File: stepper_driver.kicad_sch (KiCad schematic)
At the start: 7 parts, among them J20 Stepper, U3 TMC2208_SILENTSTEPSTICK

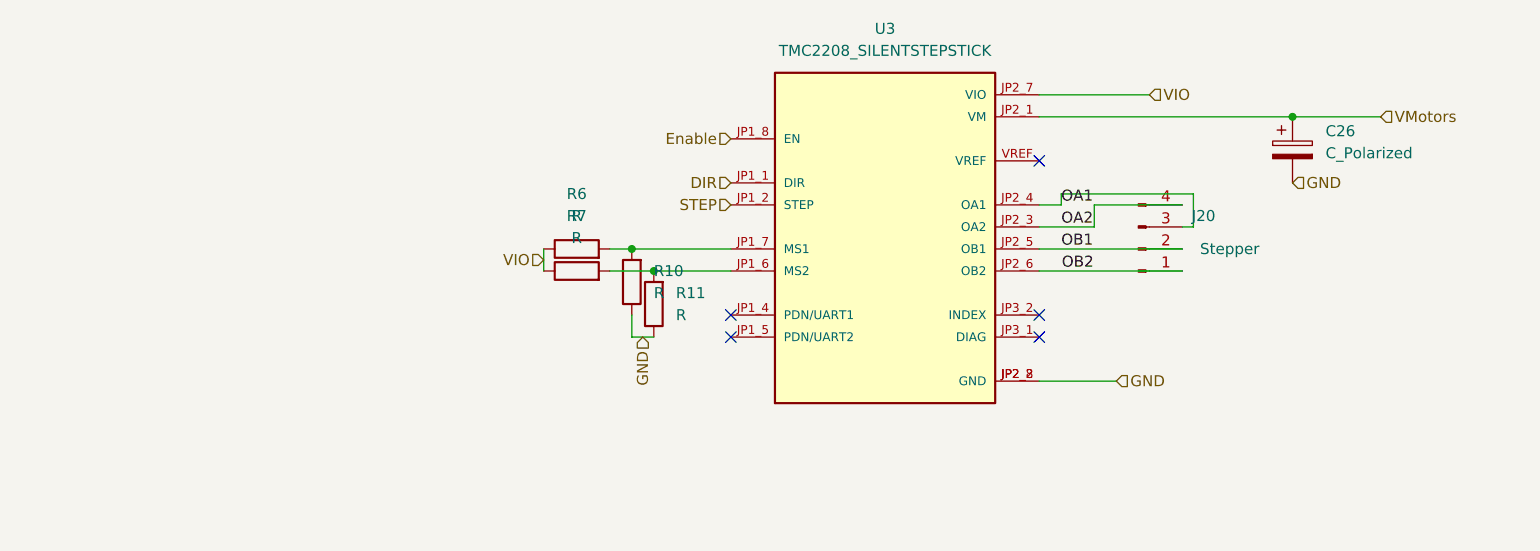
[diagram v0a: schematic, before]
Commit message: fix warnings + add internal layers + add Uart to steppers (TX only
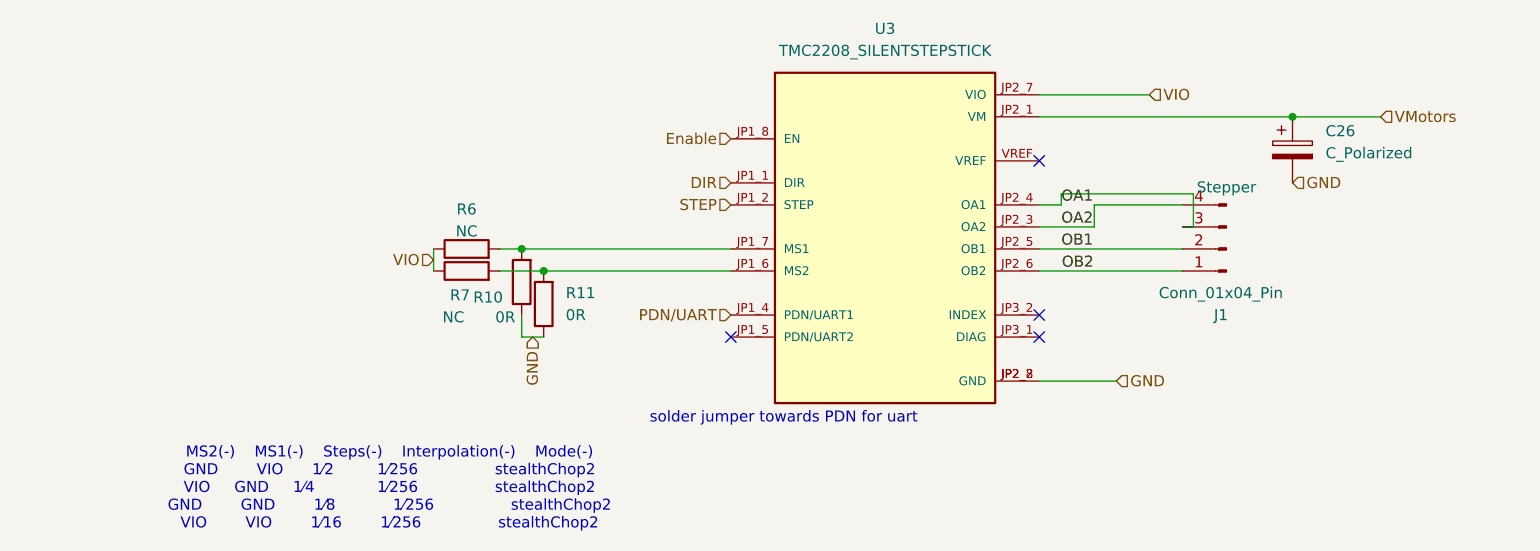
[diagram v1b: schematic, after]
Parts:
- removed J20: Stepper, Connector_JST:JST_XH_B4B-XH-A_1x04_P2.50mm_Vertical, symbol Connector:Conn_01x04_Male
- added J1: Conn_01x04_Pin, Connector_JST:JST_XH_B4B-XH-A_1x04_P2.50mm_Vertical, symbol Connector:Conn_01x04_Pin
- R10, R11: value R -> 0R
- R6, R7: value R -> NC
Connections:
- net OA1: now also J1.3 (Pin_3)
- net OA2: now also J1.4 (Pin_4)
- net OB1: now also J1.2 (Pin_2)
- net OB2: now also J1.1 (Pin_1)
- net PDN/UART: now reaches U3.JP1_4 (PDN/UART1)
- no-connect marks 5 -> 4
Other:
- note added: "MS2(-) MS1(-) Steps(-) Interpolation(-) Mode(-) GND VIO 1⁄2 1⁄256 stealthChop2 VIO GND 1⁄4 1⁄256 stealthChop2 GND GND 1⁄8 1⁄256 stealthChop2 VIO VIO 1⁄16 1⁄256 stealthChop2"
- note added: "solder jumper towards PDN for uart"
- moved on the sheet: R10, R11, R6, R7

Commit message: Add BOM
Add LCSC reference and correct few footprint acording bom
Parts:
- C26: LCSC# (none) -> C398835
- J1: LCSC# (none) -> C595709
- R10, R11: LCSC# (none) -> C21189
- U3: Availability In Stock -> (none); Check_prices https://www.snapeda.com/parts/TMC2208%20SILENTSTEPSTICK/Tri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 -> (none); MANUFACTURER Trinamic Motion -> (none); MF Trinamic Motion -> (none); MP TMC2208 SILENTSTEPSTICK -> (none); Package None -> (none); Price None -> (none); SnapEDA_Link https://www.snapeda.com/parts/TMC2208%20SILENTSTEPSTICK/Tri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 -> (none)
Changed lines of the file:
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@@
 	(label "OB2"
 		(at 130.8735 80.01 0)
-		(fields_autoplaced yes)
 		(effects
 			(font
@@
 	(label "OA1"
 		(at 130.81 72.39 0)
-		(fields_autoplaced yes)
 		(effects
 			(font
@@
 	(label "OA2"
 		(at 130.81 74.93 0)
-		(fields_autoplaced yes)
 		(effects
 			(font
@@
 	(label "OB1"
 		(at 130.81 77.47 0)
-		(fields_autoplaced yes)
 		(effects
 			(font
@@
 		(shape input)
 		(at 92.71 85.09 180)
-		(fields_autoplaced yes)
 		(effects
 			(font
@@
 		(shape input)
 		(at 157.48 69.85 0)
-		(fields_autoplaced yes)
 		(effects
 			(font
@@
 		(shape input)
 		(at 92.71 64.77 180)
-		(fields_autoplaced yes)
 		(effects
 			(font
@@
 		(shape input)
 		(at 140.97 59.69 0)
-		(fields_autoplaced yes)
 		(effects
 			(font
@@
 		(shape input)
 		(at 92.71 72.39 180)
-		(fields_autoplaced yes)
 		(effects
 			(font
@@
 		(shape input)
 		(at 58.42 78.74 180)
-		(fields_autoplaced yes)
 		(effects
 			(font
@@
 		(shape input)
 		(at 92.71 69.85 180)
-		(fields_autoplaced yes)
 		(effects
 			(font
@@
 		(shape input)
 		(at 69.85 87.63 270)
-		(fields_autoplaced yes)
 		(effects
 			(font
@@
 		(shape input)
 		(at 167.64 62.23 0)
-		(fields_autoplaced yes)
 		(effects
 			(font
@@
 		(shape input)
 		(at 137.16 92.71 0)
-		(fields_autoplaced yes)
 		(effects
 			(font
@@
 			)
 		)
+		(property "LCSC#" "C398835"
+			(at 157.48 66.04 0)
+			(effects
+				(font
+					(size 1.27 1.27)
+				)
+				(hide yes)
+			)
+		)
 		(pin "1"
 		)
@@
 		)
 		(property "Description" ""
+			(at 62.23 80.01 0)
+			(effects
+				(font
+					(size 1.27 1.27)
+				)
+				(hide yes)
+			)
+		)
+		(property "LCSC#" ""
 			(at 62.23 80.01 0)
 			(effects
@@
 			)
 		)
+		(property "LCSC#" "C21189"
+			(at 71.12 83.82 0)
+			(effects
+				(font
+					(size 1.27 1.27)
+				)
+				(hide yes)
+			)
+		)
 		(pin "1"
 		)
@@
 			)
 		)
-		(property "MF" "Trinamic Motion"
+		(property "LCSC#" ""
 			(at 110.49 74.93 0)
 			(effects
@@
 					(size 1.27 1.27)
 				)
-				(justify bottom)
-				(hide yes)
-			)
-		)
-		(property "Package" "None"
-			(at 110.49 74.93 0)
-			(effects
-				(font
-					(size 1.27 1.27)
-				)
-				(justify bottom)
-				(hide yes)
-			)
-		)
-		(property "Price" "None"
-			(at 110.49 74.93 0)
-			(effects
-				(font
-					(size 1.27 1.27)
-				)
-				(justify bottom)
-				(hide yes)
-			)
-		)
-		(property "Check_prices" "https://www.snapeda.com/parts/TMC2208%20SILENTSTEPSTICK/Trinamic+Motion+Control+GmbH/view-part/?ref=eda"
-			(at 110.49 74.93 0)
-			(effects
-				(font
-					(size 1.27 1.27)
-				)
-				(justify bottom)
-				(hide yes)
-			)
-		)
-		(property "SnapEDA_Link" "https://www.snapeda.com/parts/TMC2208%20SILENTSTEPSTICK/Trinamic+Motion+Control+GmbH/view-part/?ref=snap"
-			(at 110.49 74.93 0)
-			(effects
-				(font
-					(size 1.27 1.27)
-				)
-				(justify bottom)
-				(hide yes)
-			)
-		)
-		(property "MP" "TMC2208 SILENTSTEPSTICK"
-			(at 110.49 74.93 0)
-			(effects
-				(font
-					(size 1.27 1.27)
-				)
-				(justify bottom)
-				(hide yes)
-			)
-		)
-		(property "Availability" "In Stock"
-			(at 110.49 74.93 0)
-			(effects
-				(font
-					(size 1.27 1.27)
-				)
-				(justify bottom)
-				(hide yes)
-			)
-		)
-		(property "MANUFACTURER" "Trinamic Motion"
-			(at 110.49 74.93 0)
-			(effects
-				(font
-					(size 1.27 1.27)
-				)
-				(justify bottom)
 				(hide yes)
 			)
@@
 			)
 		)
+		(property "LCSC#" "C21189"
+			(at 68.58 81.28 0)
+			(effects
+				(font
+					(size 1.27 1.27)
+				)
+				(hide yes)
+			)
+		)
 		(pin "1"
 		)
@@
 			)
 		)
+		(property "LCSC#" ""
+			(at 62.23 77.47 0)
+			(effects
+				(font
+					(size 1.27 1.27)
+				)
+				(hide yes)
+			)
+		)
 		(pin "1"
 		)
@@
 			(at 149.86 77.47 0)
 			(effects
+				(font
+					(size 1.27 1.27)
+				)
+				(hide yes)
+			)
+		)
+		(property "LCSC#" "C595709"
+			(at 149.86 77.47 0)
+			(effects

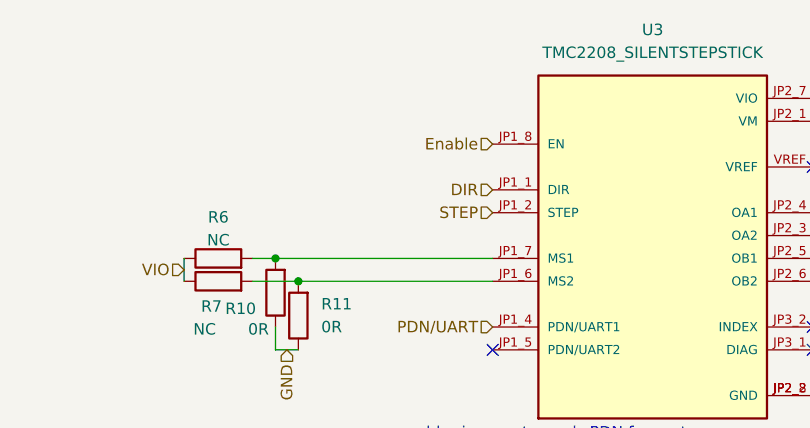
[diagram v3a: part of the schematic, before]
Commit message: fix error + add fuse/resistor choice servo DCDC vin = 12V or 24V
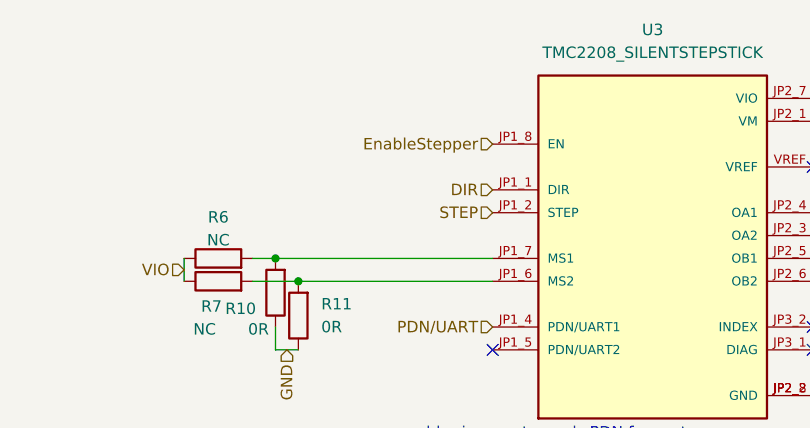
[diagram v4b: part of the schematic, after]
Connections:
- net Enable renamed EnableStepper
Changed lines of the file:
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@@
 		)
 	)
-	(hierarchical_label "Enable"
+	(hierarchical_label "EnableStepper"
 		(shape input)
 		(at 92.71 64.77 180)

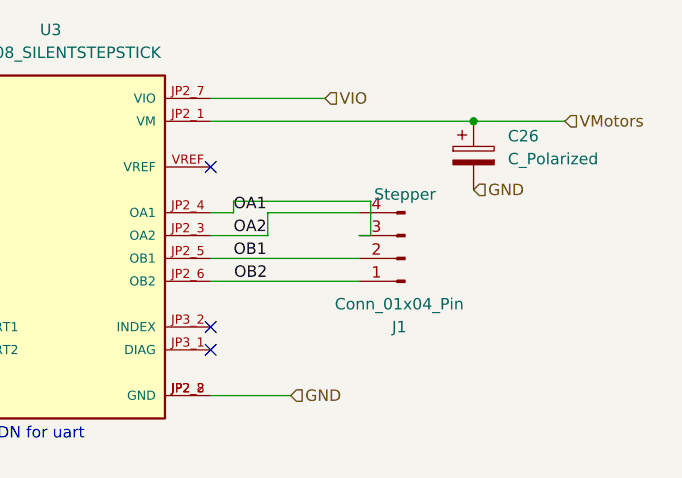
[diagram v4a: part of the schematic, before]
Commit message: update to Kicad 9 + small fixes
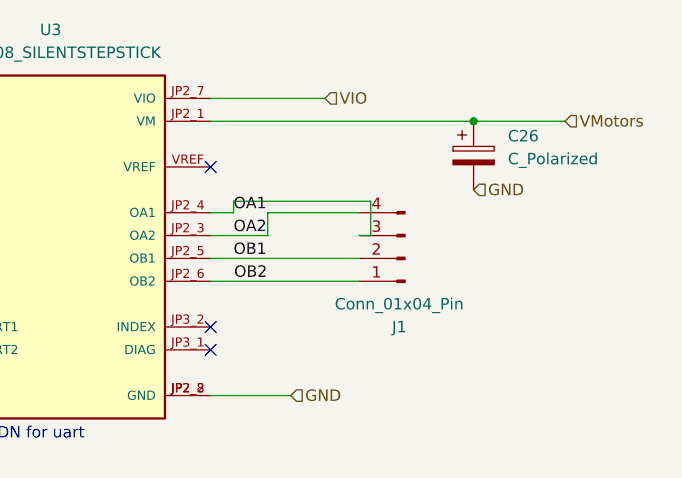
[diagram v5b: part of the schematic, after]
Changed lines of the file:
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@@
 (kicad_sch
-	(version 20231120)
+	(version 20250114)
 	(generator "eeschema")
-	(generator_version "8.0")
+	(generator_version "9.0")
 	(paper "A4")
+	(text "solder jumper towards PDN for uart"
+		(exclude_from_sim no)
+		(at 98.806 97.028 0)
+		(effects
+			(font
+				(size 1.27 1.27)
+			)
+		)
+	)
+	(text "MS2(-)	MS1(-)	Steps(-)	Interpolation(-)	Mode(-)\nGND	    VIO  	1⁄2     	1⁄256	            stealthChop2\nVIO 	GND 	1⁄4	     	1⁄256				stealthChop2\nGND		GND		1⁄8			1⁄256				stealthChop2\nVIO		VIO		1⁄16		1⁄256				stealthChop2"
+		(exclude_from_sim no)
+		(at 53.34 105.156 0)
+		(effects
+			(font
+				(size 1.27 1.27)
+			)
+		)
+	)
 	(junction
 		(at 157.48 62.23)
@@
 			(width 0)
 			(type default)
-		)
-	)
-	(text "solder jumper towards PDN for uart"
-		(exclude_from_sim no)
-		(at 98.806 97.028 0)
-		(effects
-			(font
-				(size 1.27 1.27)
-			)
-		)
-	)
-	(text "MS2(-)	MS1(-)	Steps(-)	Interpolation(-)	Mode(-)\nGND	    VIO  	1⁄2     	1⁄256	            stealthChop2\nVIO 	GND 	1⁄4	     	1⁄256				stealthChop2\nGND		GND		1⁄8			1⁄256				stealthChop2\nVIO		VIO		1⁄16		1⁄256				stealthChop2"
-		(exclude_from_sim no)
-		(at 53.34 105.156 0)
-		(effects
-			(font
-				(size 1.27 1.27)
-			)
 		)
 	)
@@
 			)
 		)
-		(property "Description" ""
+		(property "Description" "Polarized capacitor"
 			(at 157.48 66.04 0)
 			(effects
@@
 			)
 		)
-		(property "Description" ""
+		(property "Description" "Resistor"
 			(at 62.23 80.01 0)
 			(effects
@@
 			)
 		)
-		(property "Description" ""
+		(property "Description" "Resistor"
 			(at 71.12 83.82 0)
 			(effects
@@
 			)
 		)
-		(property "Description" ""
+		(property "Description" "Resistor"
 			(at 68.58 81.28 0)
 			(effects
@@
 			)
 		)
-		(property "Description" ""
+		(property "Description" "Resistor"
 			(at 62.23 77.47 0)
 			(effects
@@
 			)
 		)
-		(property "Datasheet" "Stepper"
+		(property "Datasheet" "~"
 			(at 149.86 70.358 0)
 			(effects

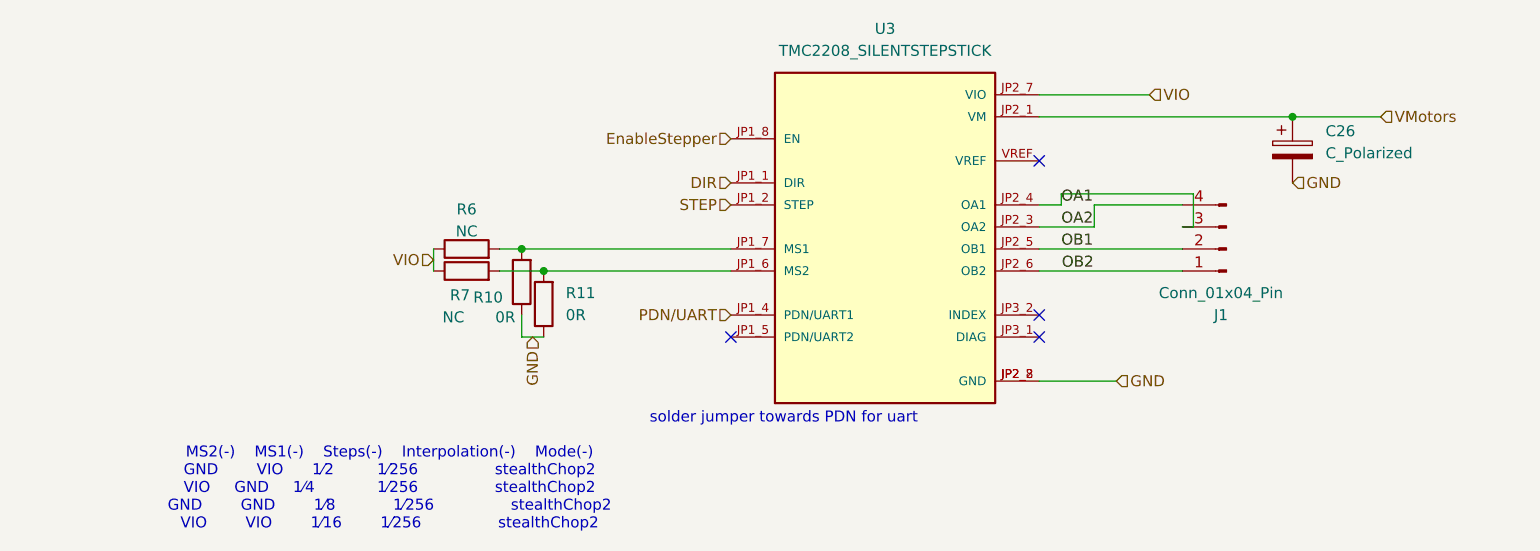
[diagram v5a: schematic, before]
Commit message: update BOM + add big capas (do not take DNP into account)
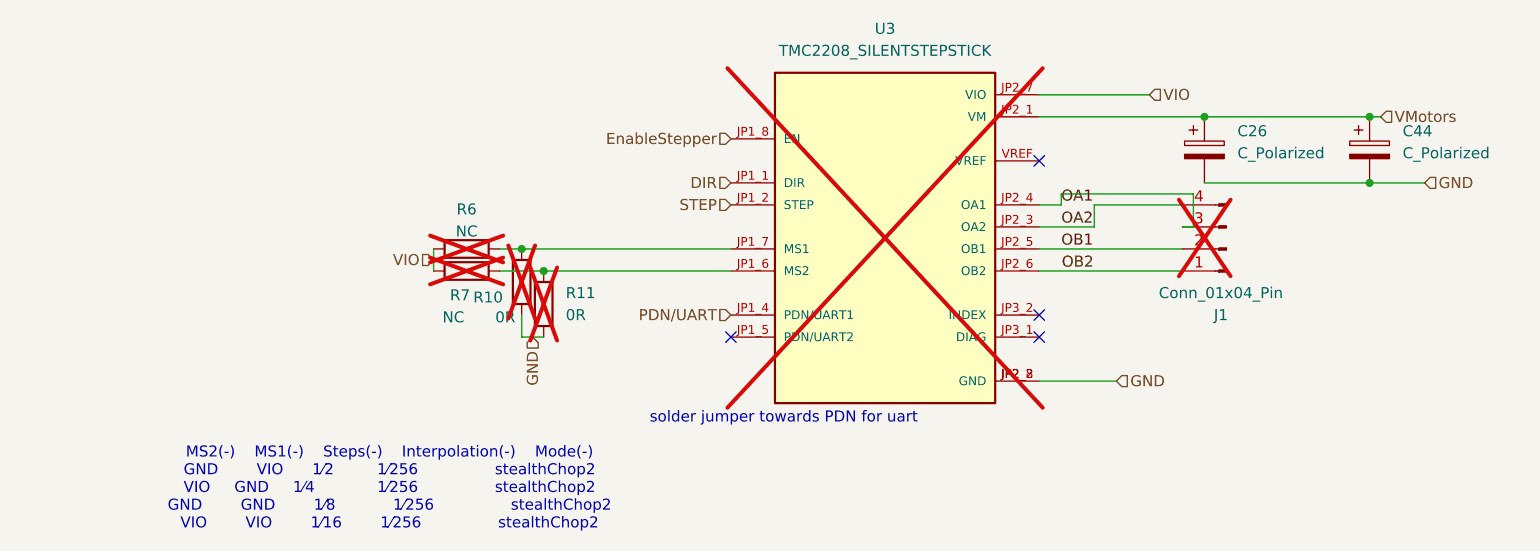
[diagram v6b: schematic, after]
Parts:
- added C44: C_Polarized, Capacitor_SMD:CP_Elec_10x10.5, symbol Device:C_Polarized
- J1, R10, R11, R6, R7, U3: now not fitted
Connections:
- net GND: now also C44.2
- net VMotors: now also C44.1
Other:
- moved on the sheet: C26
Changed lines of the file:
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@@
 	)
 	(junction
-		(at 157.48 62.23)
+		(at 166.37 69.85)
+		(diameter 0)
+		(color 0 0 0 0)
+	)
+	(junction
+		(at 166.37 62.23)
 		(diameter 0)
 		(color 0 0 0 0)
@@
 		(color 0 0 0 0)
 	)
+	(junction
+		(at 147.32 62.23)
+		(diameter 0)
+		(color 0 0 0 0)
+	)
 	(no_connect
 		(at 128.27 67.31)
@@
 	(wire
 		(pts
-			(xy 157.48 62.23) (xy 167.64 62.23)
-		)
-		(stroke
-			(width 0)
-			(type default)
-		)
-	)
-	(wire
-		(pts
 			(xy 66.04 77.47) (xy 68.58 77.47)
 		)
@@
 	(wire
 		(pts
+			(xy 172.72 69.85) (xy 166.37 69.85)
+		)
+		(stroke
+			(width 0)
+			(type default)
+		)
+	)
+	(wire
+		(pts
 			(xy 128.27 74.93) (xy 134.62 74.93)
 		)
@@
 	(wire
 		(pts
+			(xy 166.37 69.85) (xy 147.32 69.85)
+		)
+		(stroke
+			(width 0)
+			(type default)
+		)
+	)
+	(wire
+		(pts
 			(xy 128.27 72.39) (xy 130.81 72.39)
 		)
@@
 	(wire
 		(pts
+			(xy 166.37 62.23) (xy 167.64 62.23)
+		)
+		(stroke
+			(width 0)
+			(type default)
+		)
+	)
+	(wire
+		(pts
 			(xy 134.62 72.39) (xy 144.78 72.39)
 		)
@@
 	(wire
 		(pts
-			(xy 128.27 62.23) (xy 157.48 62.23)
+			(xy 128.27 62.23) (xy 147.32 62.23)
 		)
 		(stroke
@@
 		(pts
 			(xy 130.81 71.12) (xy 146.05 71.12)
+		)
+		(stroke
+			(width 0)
+			(type default)
+		)
+	)
+	(wire
+		(pts
+			(xy 147.32 62.23) (xy 166.37 62.23)
 		)
 		(stroke
@@
 	(hierarchical_label "GND"
 		(shape input)
-		(at 157.48 69.85 0)
+		(at 172.72 69.85 0)
 		(effects
 			(font
@@
 	(symbol
 		(lib_id "Device:C_Polarized")
-		(at 157.48 66.04 0)
+		(at 147.32 66.04 0)
 		(unit 1)
 		(exclude_from_sim no)
@@
 		(fields_autoplaced yes)
 		(property "Reference" "C26"
-			(at 161.29 63.8809 0)
+			(at 151.13 63.8809 0)
 			(effects
 				(font
@@
 		)
 		(property "Value" "C_Polarized"
-			(at 161.29 66.4209 0)
+			(at 151.13 66.4209 0)
 			(effects
 				(font
@@
 		)
 		(property "Footprint" "Capacitor_THT:CP_Radial_D10.0mm_P5.00mm"
-			(at 158.4452 69.85 0)
+			(at 148.2852 69.85 0)
 			(effects
 				(font
@@
 		)
 		(property "Datasheet" "~"
-			(at 157.48 66.04 0)
+			(at 147.32 66.04 0)
 			(effects
 				(font
@@
 		)
 		(property "Description" "Polarized capacitor"
-			(at 157.48 66.04 0)
+			(at 147.32 66.04 0)
 			(effects
 				(font
@@
 		)
 		(property "LCSC#" "C398835"
-			(at 157.48 66.04 0)
+			(at 147.32 66.04 0)
 			(effects
 				(font
@@
 		(in_bom yes)
 		(on_board yes)
-		(dnp no)
+		(dnp yes)
 		(property "Reference" "R7"
 			(at 61.468 82.804 90)
@@
 		(in_bom yes)
 		(on_board yes)
-		(dnp no)
+		(dnp yes)
 		(fields_autoplaced yes)
 		(property "Reference" "R11"
@@
 		(in_bom yes)
 		(on_board yes)
-		(dnp no)
+		(dnp yes)
 		(fields_autoplaced yes)
 		(property "Reference" "U3"
@@
 		(in_bom yes)
 		(on_board yes)
-		(dnp no)
+		(dnp yes)
 		(property "Reference" "R10"
 			(at 62.992 83.058 0)
@@
 		(in_bom yes)
 		(on_board yes)
-		(dnp no)
+		(dnp yes)
 		(property "Reference" "R6"
 			(at 62.23 72.898 90)
@@
 				(path "/e63e39d7-6ac0-4ffd-8aa3-1841a4541b55/f86a3d70-fa31-4725-b330-81e2f5dad2cc"
 					(reference "R13")
+					(unit 1)
+				)
+			)
+		)
+	)
+	(symbol
+		(lib_id "Device:C_Polarized")
+		(at 166.37 66.04 0)
+		(unit 1)
+		(exclude_from_sim no)
+		(in_bom yes)
+		(on_board yes)
+		(dnp no)
+		(fields_autoplaced yes)
+		(property "Reference" "C44"
+			(at 170.18 63.8809 0)
+			(effects
+				(font
+					(size 1.27 1.27)
+				)
+				(justify left)
+			)
+		)
+		(property "Value" "C_Polarized"
+			(at 170.18 66.4209 0)
+			(effects
+				(font
+					(size 1.27 1.27)
+				)
+				(justify left)
+			)
+		)
+		(property "Footprint" "Capacitor_SMD:CP_Elec_10x10.5"
+			(at 167.3352 69.85 0)
+			(effects
+				(font
+					(size 1.27 1.27)
+				)
+				(hide yes)
+			)
+		)
+		(property "Datasheet" "~"
+			(at 166.37 66.04 0)
+			(effects
+				(font
+					(size 1.27 1.27)
+				)
+				(hide yes)
+			)
+		)
+		(property "Description" "Polarized capacitor"
+			(at 166.37 66.04 0)
+			(effects
+				(font
+					(size 1.27 1.27)
+				)
+				(hide yes)
+			)
+		)
+		(property "LCSC#" "C398835"
+			(at 166.37 66.04 0)
+			(effects
+				(font
+					(size 1.27 1.27)
+				)
+				(hide yes)
+			)
+		)
+		(pin "1"
+		)
+		(pin "2"
+		)
+		(instances
+			(project "carte_servo"
+				(path "/e63e39d7-6ac0-4ffd-8aa3-1841a4541b55/4bdf100d-7e35-4013-89a2-8f86fd135421"
+					(reference "C44")
+					(unit 1)
+				)
+				(path "/e63e39d7-6ac0-4ffd-8aa3-1841a4541b55/f86a3d70-fa31-4725-b330-81e2f5dad2cc"
+					(reference "C45")
 					(unit 1)
 				)
@@
 		(in_bom yes)
 		(on_board yes)
-		(dnp no)
+		(dnp yes)
 		(property "Reference" "J1"
 			(at 149.225 85.09 0)
